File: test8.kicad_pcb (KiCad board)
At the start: 2 copper layers, 28.5 x 23.5 mm, 3 parts, among them J1 Conn_01x02_Pin, U1 74HC165, U2 74HC165

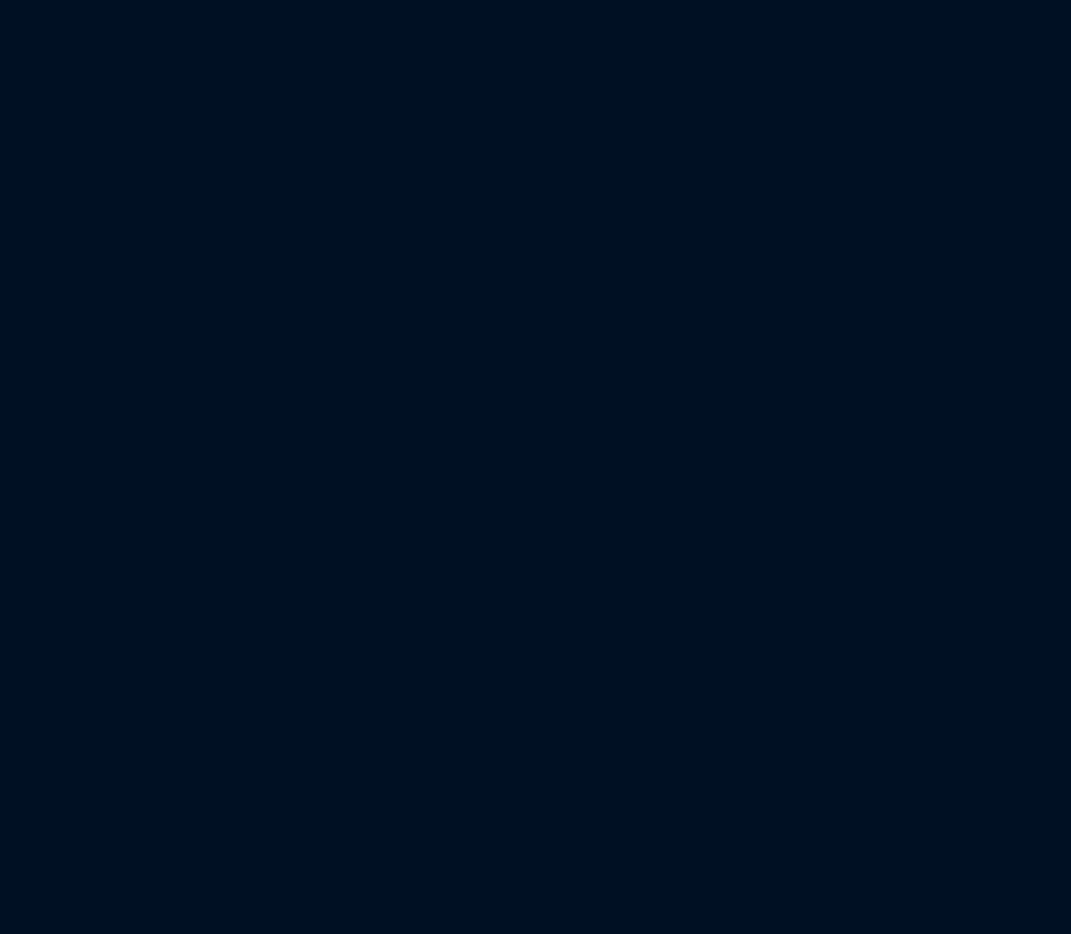
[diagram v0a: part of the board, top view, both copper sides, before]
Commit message: esp32wrom process
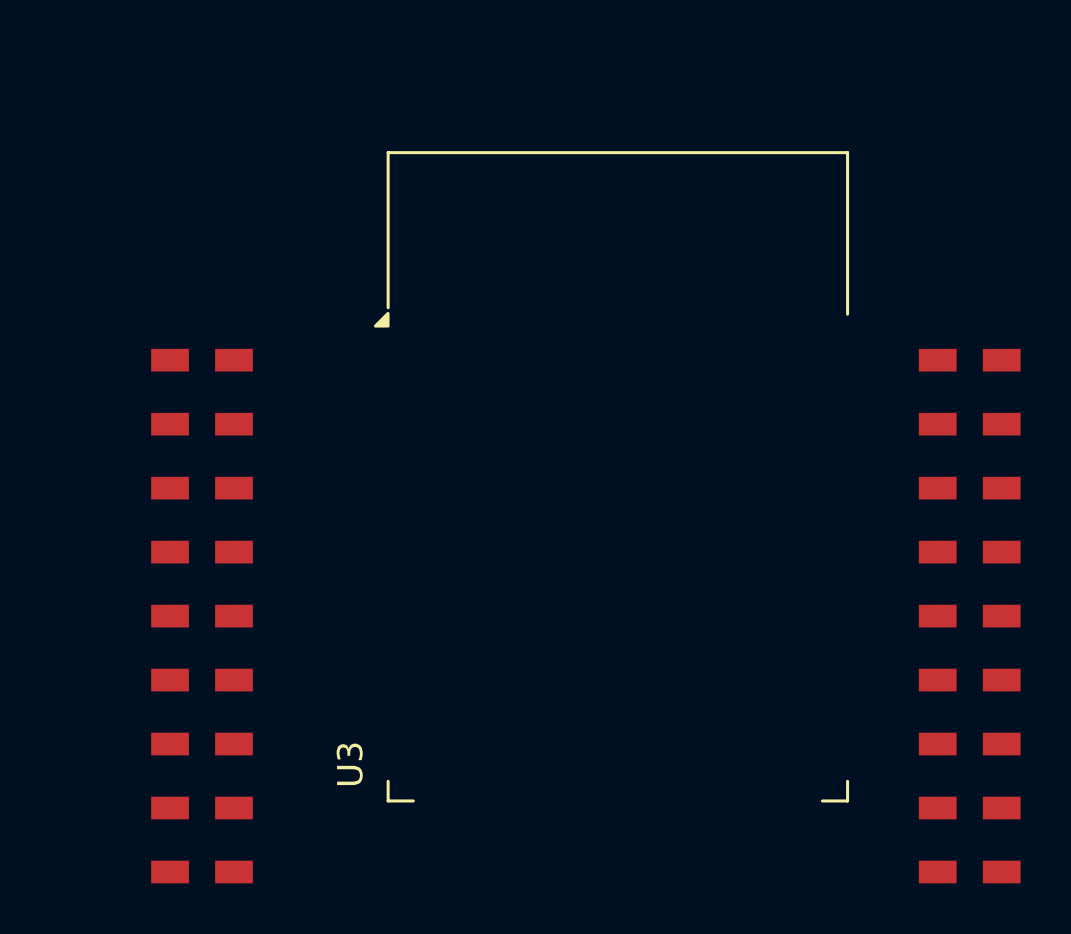
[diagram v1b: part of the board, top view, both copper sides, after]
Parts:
- added U3: ESP32-WROOM-32, main:ESP32-WROOM-32, F.Cu at (145.8, 108.8)

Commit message: process
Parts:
- moved U1 26.1 mm to (120.5, 108.0)
- moved U2 14.2 mm to (120.2, 95.1)
- moved J1 11.2 mm to (112.5, 93.5), turned to 180 degrees
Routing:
- net GND: track 30.7 -> 0.00 mm
- net +3.3V: track 14.4 -> 0.00 mm
- removed copper zone on B.Cu, net GND
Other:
- board size 28.5 x 23.5 mm -> 58 x 46 mm

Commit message: xz
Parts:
- added U4: 74HC595, Package_DIP:DIP-16_W7.62mm_LongPads, F.Cu at (195.4, 96.7)
- added U5: 74HC595, Package_DIP:DIP-16_W7.62mm_LongPads, F.Cu at (177.2, 96.1)
- moved U2 17.2 mm to (123.5, 112.0)
- moved U3 11.8 mm to (153.0, 99.5)
- moved U1 11.4 mm to (123.5, 97.0)
- moved J1 3.16 mm to (113.5, 90.5)
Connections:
- U1 pad 1: unconnected-(U1-~{PL}-Pad1) -> CS_165
- U1 pad 10: unconnected-(U1-DS-Pad10) -> Net-(U1-DS)
- U1 pad 15: unconnected-(U1-~{CE}-Pad15) -> GND
- U1 pad 2: unconnected-(U1-CP-Pad2) -> CLK_165
- U1 pad 9: unconnected-(U1-Q7-Pad9) -> MISO_165
- U2 pad 1: unconnected-(U2-~{PL}-Pad1) -> CS_165
- U2 pad 15: unconnected-(U2-~{CE}-Pad15) -> GND
- U2 pad 2: unconnected-(U2-CP-Pad2) -> CLK_165
- U2 pad 9: unconnected-(U2-Q7-Pad9) -> Net-(U1-DS)
- U3 pad 13: unconnected-(U3-IO14-Pad13) -> Net-(U3-IO14)
- U3 pad 16: unconnected-(U3-IO13-Pad16) -> Net-(U3-IO13)
- U3 pad 23: unconnected-(U3-IO15-Pad23) -> Net-(U3-IO15)
- U3 pad 30: unconnected-(U3-IO18-Pad30) -> CLK_165
- U3 pad 31: unconnected-(U3-IO19-Pad31) -> MISO_165
- U3 pad 5: unconnected-(U3-SENSOR_VN-Pad5) -> CS_165
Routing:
- net GND: track 0.00 -> 196.8 mm
- net +3.3V: track 0.00 -> 34.6 mm
- net CS_165: track 0.00 -> 30.1 mm
- net +5V: track 0.00 -> 22.5 mm
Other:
- board size 58 x 46 mm -> 100 x 46 mm

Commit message: 595+165+topor
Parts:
- added J1: Conn_01x10_Socket, main:PinHeader_2x05_P2.00mm_Vertical, F.Cu at (112.0, 92.5)
- added J2: Conn_01x10_Socket, main:PinHeader_2x05_P2.00mm_Vertical, F.Cu at (112.0, 108.0)
- added J4: Conn_01x10_Socket, main:PinHeader_2x05_P2.00mm_Vertical, F.Cu at (196.5, 130.0)
- added J5: Conn_01x10_Socket, main:PinHeader_2x05_P2.00mm_Vertical, F.Cu at (197.5, 102.0)
- J3: renamed from J1; footprint Connector_PinHeader_2.54mm:PinHeader_1x02_P2.54mm_Vertical -> main:PinHeader_1x02_P2.54mm_Vertical
- moved U4 39.7 mm to (186.3, 135.4), turned to 180 degrees
- moved U5 14.4 mm to (186.0, 107.5), turned to 180 degrees
- moved J3 5.10 mm to (114.5, 85.5), turned to -90 degrees
- moved U1 0.50 mm to (123.5, 96.5), turned to 0 degrees
- moved U2 0.50 mm to (123.5, 111.5), turned to 0 degrees
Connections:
- U1 pad 1: CS_165 -> CLK_165
- U1 pad 11: unconnected-(U1-D0-Pad11) -> Net-(J1-Pin_1)
- U1 pad 12: unconnected-(U1-D1-Pad12) -> Net-(J1-Pin_2)
- U1 pad 13: unconnected-(U1-D2-Pad13) -> Net-(J1-Pin_3)
- U1 pad 14: unconnected-(U1-D3-Pad14) -> Net-(J1-Pin_4)
- U1 pad 2: CLK_165 -> CS_165
- U1 pad 3: unconnected-(U1-D4-Pad3) -> Net-(J1-Pin_5)
- U1 pad 4: unconnected-(U1-D5-Pad4) -> Net-(J1-Pin_6)
- U1 pad 5: unconnected-(U1-D6-Pad5) -> Net-(J1-Pin_7)
- U1 pad 6: unconnected-(U1-D7-Pad6) -> Net-(J1-Pin_8)
- U2 pad 11: unconnected-(U2-D0-Pad11) -> Net-(J2-Pin_1)
- U2 pad 12: unconnected-(U2-D1-Pad12) -> Net-(J2-Pin_2)
- U2 pad 13: unconnected-(U2-D2-Pad13) -> Net-(J2-Pin_3)
- U2 pad 14: unconnected-(U2-D3-Pad14) -> Net-(J2-Pin_4)
- U2 pad 3: unconnected-(U2-D4-Pad3) -> Net-(J2-Pin_5)
- U2 pad 4: unconnected-(U2-D5-Pad4) -> Net-(J2-Pin_6)
- U2 pad 5: unconnected-(U2-D6-Pad5) -> Net-(J2-Pin_7)
- U2 pad 6: unconnected-(U2-D7-Pad6) -> Net-(J2-Pin_8)
- U4 pad 1: unconnected-(U4-QB-Pad1) -> Net-(J4-Pin_2)
- U4 pad 15: unconnected-(U4-QA-Pad15) -> Net-(J4-Pin_1)
- U4 pad 2: unconnected-(U4-QC-Pad2) -> Net-(J4-Pin_3)
- U4 pad 3: unconnected-(U4-QD-Pad3) -> Net-(J4-Pin_4)
- U4 pad 4: unconnected-(U4-QE-Pad4) -> Net-(J4-Pin_5)
- U4 pad 5: unconnected-(U4-QF-Pad5) -> Net-(J4-Pin_6)
- U4 pad 6: unconnected-(U4-QG-Pad6) -> Net-(J4-Pin_7)
- U4 pad 7: unconnected-(U4-QH-Pad7) -> Net-(J5-Pin_1)
- U5 pad 1: unconnected-(U5-QB-Pad1) -> Net-(J5-Pin_3)
- U5 pad 15: unconnected-(U5-QA-Pad15) -> Net-(J5-Pin_2)
- U5 pad 2: unconnected-(U5-QC-Pad2) -> Net-(J5-Pin_4)
- U5 pad 3: unconnected-(U5-QD-Pad3) -> Net-(J5-Pin_5)
- U5 pad 4: unconnected-(U5-QE-Pad4) -> Net-(J5-Pin_6)
- U5 pad 5: unconnected-(U5-QF-Pad5) -> Net-(J5-Pin_7)
- U5 pad 6: unconnected-(U5-QG-Pad6) -> Net-(J5-Pin_8)
- U5 pad 7: unconnected-(U5-QH-Pad7) -> Net-(J5-Pin_9)
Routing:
- net GND: track 196.8 -> 0.00 mm
- net +3.3V: track 34.6 -> 0.00 mm
- net CS_165: track 30.1 -> 0.00 mm
- net +5V: track 22.5 -> 0.00 mm
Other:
- board size 100 x 46 mm -> 100 x 66.5 mm

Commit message: вариант 1
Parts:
- added C1: , C1, B.Cu at (183.8, 88.5)
- added C2: , C2, F.Cu at (101.7, 75.0)
- added C3: , C3, B.Cu at (152.3, 67.5)
- added C4: , C4, F.Cu at (112.3, 67.5)
- added C5: , C5, B.Cu at (109.3, 75.0)
- added C6: , C6, B.Cu at (99.8, 87.5)
- added C7: , C7, B.Cu at (100.8, 108.0)
- added J6: , J6, F.Cu at (159.8, 82.0)
- added J7: , J7, F.Cu at (184.8, 99.5)
- added J8: , J8, F.Cu at (184.3, 78.0)
- added U6: , U6, F.Cu at (176.1, 83.8)
- J1: value Conn_01x10_Socket -> (none); footprint main:PinHeader_2x05_P2.00mm_Vertical -> J1
- J2: value Conn_01x10_Socket -> (none); footprint main:PinHeader_2x05_P2.00mm_Vertical -> J2
- J3: value Conn_01x02_Pin -> (none); footprint main:PinHeader_1x02_P2.54mm_Vertical -> J3
- J4: value Conn_01x10_Socket -> (none); footprint main:PinHeader_2x05_P2.00mm_Vertical -> J4
- J5: value Conn_01x10_Socket -> (none); footprint main:PinHeader_2x05_P2.00mm_Vertical -> J5
- U1: value 74HC165 -> (none); footprint Package_SO:SOP-16_4.55x10.3mm_P1.27mm -> U1
- U2: value 74HC165 -> (none); footprint Package_SO:SOP-16_4.55x10.3mm_P1.27mm -> U2
- U3: value ESP32-WROOM-32 -> (none); footprint main:ESP32-WROOM-32 -> U3; moved to B.Cu
- U4: value 74HC595 -> (none); footprint Package_DIP:DIP-16_W7.62mm_LongPads -> U4
- U5: value 74HC595 -> (none); footprint Package_DIP:DIP-16_W7.62mm_LongPads -> U5
- moved J4 69.9 mm to (163.3, 68.5), turned to -90 degrees
- moved U4 69.9 mm to (138.8, 84.1), turned to 0 degrees
- moved U3 45.9 mm to (110.8, 81.5), turned to 90 degrees
- moved J5 43.3 mm to (163.3, 75.5), turned to -90 degrees
- moved J3 24.3 mm to (100.8, 65.5)
- moved J2 15.3 mm to (101.8, 119.5), turned to 180 degrees
- moved J1 12.5 mm to (101.3, 99.0), turned to 180 degrees
- moved U1 12.2 mm to (111.5, 94.0), turned to 180 degrees
- moved U2 11.0 mm to (112.8, 114.0), turned to 180 degrees
- moved U5 10.1 mm to (176.1, 109.8)
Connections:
- J3 pad 1: GND -> +5V
- J3 pad 2: +3.3V -> GND
- J4 pad 3: Net-(J4-Pin_3) -> GND
- J5 pad 1: Net-(J5-Pin_1) -> +5V
- J5 pad 2: Net-(J5-Pin_2) -> H34P
- J5 pad 3: Net-(J5-Pin_3) -> GND
- U3 pad 3: unconnected-(U3-EN-Pad3) -> +5V
- U4 pad 1: Net-(J4-Pin_2) -> GND
- U4 pad 10: +5V -> unconnected-(U4-IO25-Pad10)
- U4 pad 11: Net-(U3-IO14) -> unconnected-(U4-IO26-Pad11)
- U4 pad 12: Net-(U3-IO15) -> unconnected-(U4-IO27-Pad12)
- U4 pad 13: GND -> Net-(U4-IO14)
- U4 pad 14: Net-(U3-IO13) -> unconnected-(U4-IO12-Pad14)
- U4 pad 16: +5V -> Net-(U4-IO13)
- U4 pad 2: Net-(J4-Pin_3) -> +3.3V
- U4 pad 3: Net-(J4-Pin_4) -> unconnected-(U4-EN-Pad3)
- U4 pad 4: Net-(J4-Pin_5) -> unconnected-(U4-SENSOR_VP-Pad4)
- U4 pad 5: Net-(J4-Pin_6) -> CS_165
- U4 pad 6: Net-(J4-Pin_7) -> unconnected-(U4-IO34-Pad6)
- U4 pad 7: Net-(J5-Pin_1) -> unconnected-(U4-IO35-Pad7)
- U4 pad 8: GND -> unconnected-(U4-IO32-Pad8)
- U4 pad 9: Net-(U4-QH') -> unconnected-(U4-IO33-Pad9)
- U5 pad 1: Net-(J5-Pin_3) -> Net-(J7-Pin_2)
- U5 pad 11: Net-(U3-IO14) -> Net-(U4-IO14)
- U5 pad 12: Net-(U3-IO15) -> Net-(U4-IO15)
- U5 pad 14: Net-(U4-QH') -> Net-(U4-IO13)
- U5 pad 15: Net-(J5-Pin_2) -> Net-(J7-Pin_1)
- U5 pad 2: Net-(J5-Pin_4) -> Net-(J7-Pin_3)
- U5 pad 3: Net-(J5-Pin_5) -> Net-(J7-Pin_4)
- U5 pad 4: Net-(J5-Pin_6) -> Net-(J7-Pin_5)
- U5 pad 5: Net-(J5-Pin_7) -> Net-(J7-Pin_6)
- U5 pad 6: Net-(J5-Pin_8) -> Net-(J7-Pin_7)
- U5 pad 7: Net-(J5-Pin_9) -> Net-(J8-Pin_1)
- U5 pad 9: unconnected-(U5-QH'-Pad9) -> Net-(U5-QH')
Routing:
- net GND: track 0.00 -> 324.7 mm, vias 0 -> 2
- net +3.3V: track 0.00 -> 249.9 mm, vias 0 -> 1
- net +5V: track 0.00 -> 246.9 mm
- net CLK_165: track 0.00 -> 110.5 mm, vias 0 -> 3
- net Net-(U4-IO14): track 0.00 -> 88.1 mm, vias 0 -> 1
- net Net-(J1-Pin_6): track 0.00 -> 82.5 mm
- net Net-(U4-IO13): track 0.00 -> 59.1 mm
- net CS_165: track 0.00 -> 59.0 mm, vias 0 -> 2
- net MISO_165: track 0.00 -> 55.4 mm
- net Net-(U4-IO15): track 0.00 -> 49.9 mm
- net Net-(J2-Pin_4): track 0.00 -> 49.1 mm, vias 0 -> 1
- net Net-(J2-Pin_1): track 0.00 -> 47.8 mm, vias 0 -> 1
- net Net-(J2-Pin_2): track 0.00 -> 43.1 mm
- net Net-(J1-Pin_2): track 0.00 -> 42.4 mm, vias 0 -> 1
- net RX433: track 0.00 -> 42.1 mm
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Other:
- board outline removed

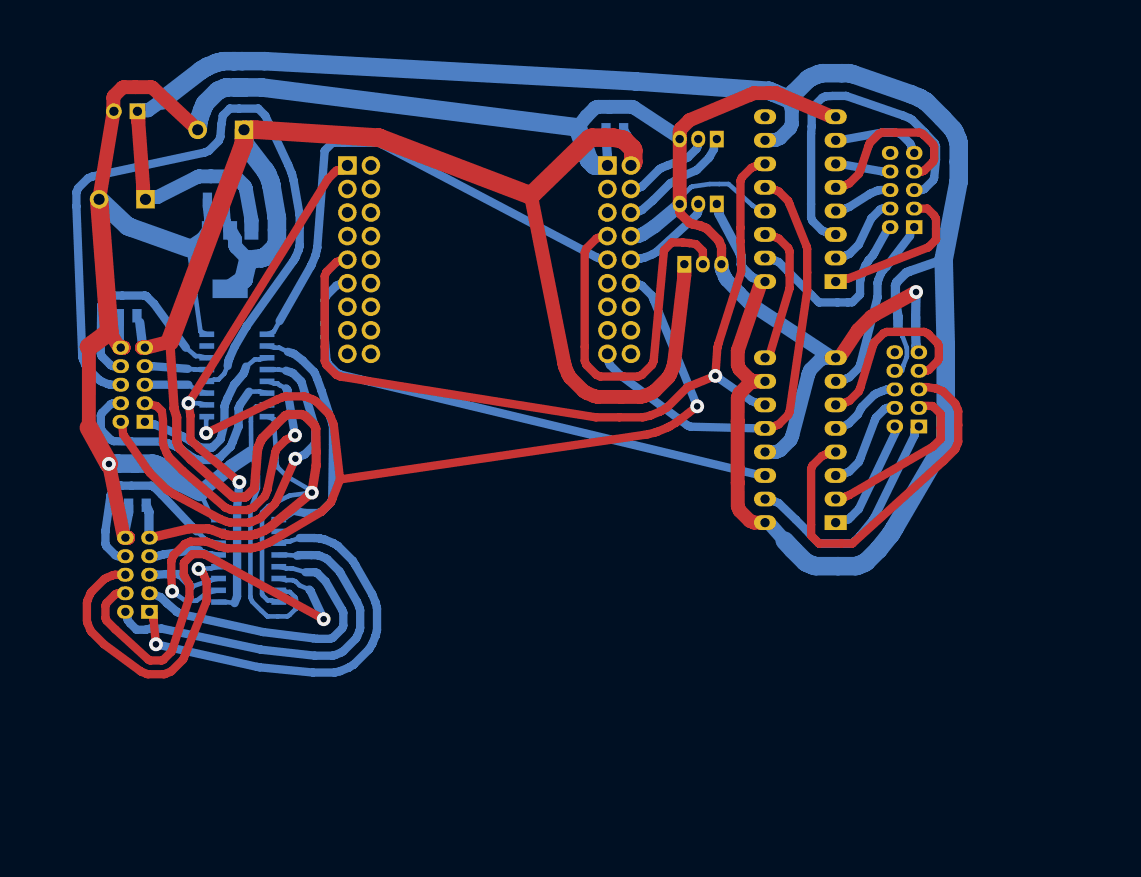
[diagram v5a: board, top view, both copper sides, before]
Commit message: Граница ПП изм слой
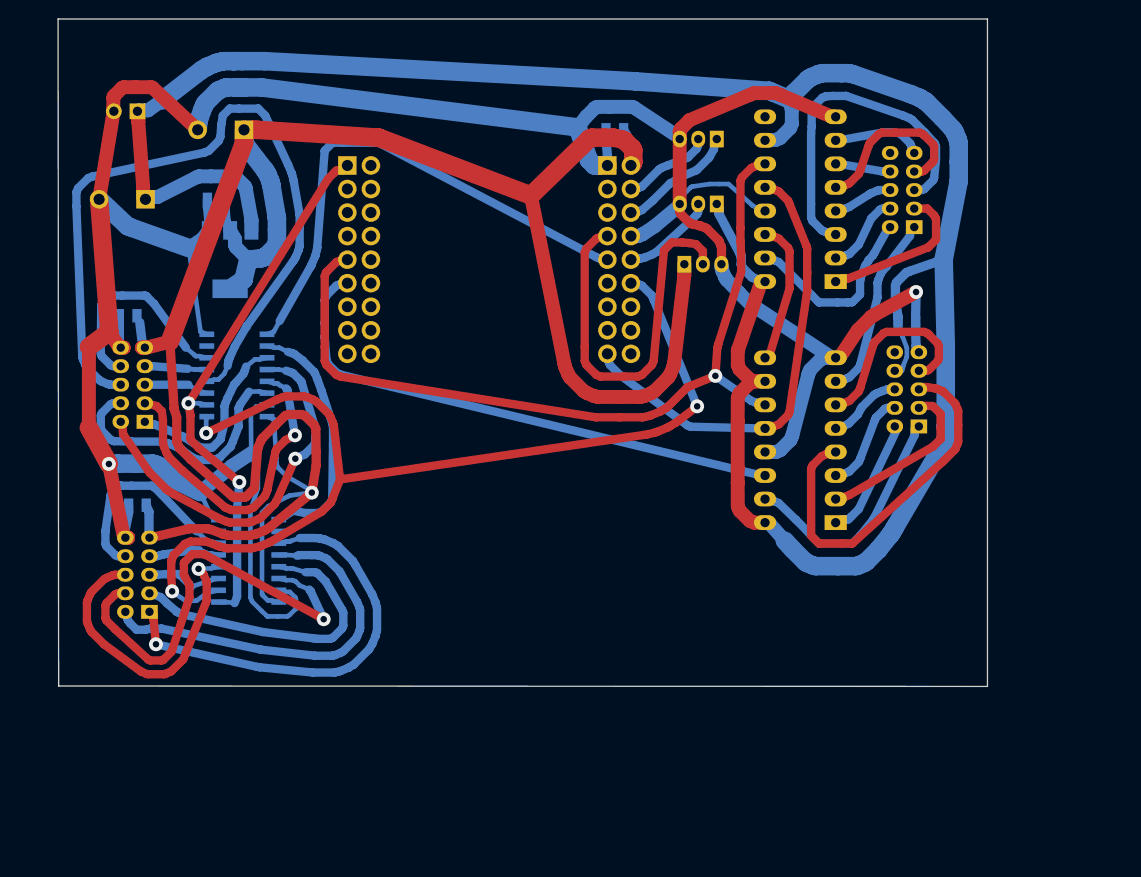
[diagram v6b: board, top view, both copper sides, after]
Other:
- board outline added: 100.3 x 72 mm
